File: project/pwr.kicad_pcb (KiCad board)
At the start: 2 copper layers, 75 x 80 mm, 113 parts, among them J101 IDC 2x8, J201 XT-IN, J202 METER, J203 XT-OUT, J301 XT-IN, J302 METER, J303 XT-OUT, J401 XT-IN, J402 METER, J403 XT-OUT, J501 XT-IN, J502 METER, J503 XT-OUT, J601 XT-IN, J602 METER, J603 XT-OUT, Q201 AON6144, Q301 AON6144, Q401 AON6144, Q501 AON6144, Q601 AON6144, U101 USBLC6-2SC6, U102 USBLC6-2SC6, U103 USBLC6-2SC6, U104 USBLC6-2SC6, U105 TMP102AIDRLR, U106 TMP102AIDRLR, U201 UCC27517DBVR, U301 UCC27517DBVR, U401 UCC27517DBVR, U501 UCC27517DBVR, U601 UCC27517DBVR

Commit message: finalizing design
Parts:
- removed kibuzzard-66D16323: G***, kibuzzard-66D16323
- added C108: 220u, Capacitor_SMD:CP_Elec_10x10.5, F.Cu at (121.0, 77.5)
- added D101: ALR, LED_SMD:LED_0805_2012Metric_Pad1.15x1.40mm_HandSolder, F.Cu at (129.5, 34.0)
- added D102: VCC, LED_SMD:LED_0805_2012Metric_Pad1.15x1.40mm_HandSolder, F.Cu at (115.5, 34.0)
- added R108: 100R, Resistor_SMD:R_0805_2012Metric_Pad1.20x1.40mm_HandSolder, F.Cu at (129.5, 36.0)
- added R109: 100R, Resistor_SMD:R_0805_2012Metric_Pad1.20x1.40mm_HandSolder, F.Cu at (115.5, 36.0)
- added TP101: TP_GND, TestPoint:TestPoint_Loop_D2.60mm_Drill1.6mm_Beaded, F.Cu at (124.0, 30.5)
- added TP201: TP_GND, TestPoint:TestPoint_Pad_D2.5mm, F.Cu at (151.0, 30.5)
- added TP301: TP_GND, TestPoint:TestPoint_Pad_D2.5mm, F.Cu at (151.0, 45.5)
- added TP401: TP_GND, TestPoint:TestPoint_Pad_D2.5mm, F.Cu at (151.0, 60.5)
- added TP501: TP_GND, TestPoint:TestPoint_Pad_D2.5mm, F.Cu at (151.0, 75.6)
- added TP601: TP_GND, TestPoint:TestPoint_Pad_D2.5mm, F.Cu at (151.0, 90.5)
- added kibuzzard-66D4F7A8: G***, kibuzzard-66D4F7A8, F.Cu at (174.2, 82.8)
- moved G102 21.0 mm to (109.0, 33.5)
- moved kibuzzard-66D08EDB 20.8 mm to (109.0, 87.5)
- moved G101 14.3 mm to (126.0, 87.5)
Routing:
- net 3V3: track 88.2 -> 123.4 mm, vias 10 -> 11
- net /ALERT_P: track 39.0 -> 54.5 mm, vias 3 -> 5
- net Net-(D102-Pad1): track 0.00 -> 2.01 mm
- net Net-(D101-Pad2): track 0.00 -> 2.01 mm
- net GND: vias 17 -> 24
- net /pwr_ch5/PGND: vias 7 -> 8
- net /pwr_ch4/PGND: vias 7 -> 8
- net /pwr_ch3/PGND: vias 7 -> 8
- net /pwr_ch2/PGND: vias 7 -> 8
- net /pwr_ch1/PGND: vias 7 -> 8
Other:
- board size 75 x 80 mm -> 75 x 77.5 mm
- board text added: "3V3"
- board text added: "JLCJLCJLCJL"
- board text added: "OTP"

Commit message: generating production files for power board
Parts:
- moved J101 28.0 mm to (121.5, 88.6)
- moved C101 28.0 mm to (134.2, 92.8)
- moved C102 28.0 mm to (132.2, 72.5)
- moved C103 28.0 mm to (132.2, 78.0)
- moved C104 28.0 mm to (132.2, 83.5)
- moved C105 28.0 mm to (132.2, 89.0)
- moved C106 28.0 mm to (140.5, 67.0)
- moved C107 28.0 mm to (140.5, 97.0)
- moved C108 28.0 mm to (126.0, 105.0)
- moved C201 28.0 mm to (144.5, 68.0)
- moved C202 28.0 mm to (140.5, 61.0)
- moved C203 28.0 mm to (148.5, 66.0)
- moved C204 28.0 mm to (148.5, 70.0)
- moved C301 28.0 mm to (144.5, 83.0)
- moved C302 28.0 mm to (140.5, 76.0)
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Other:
- board text added: "D = 3.2 mm"

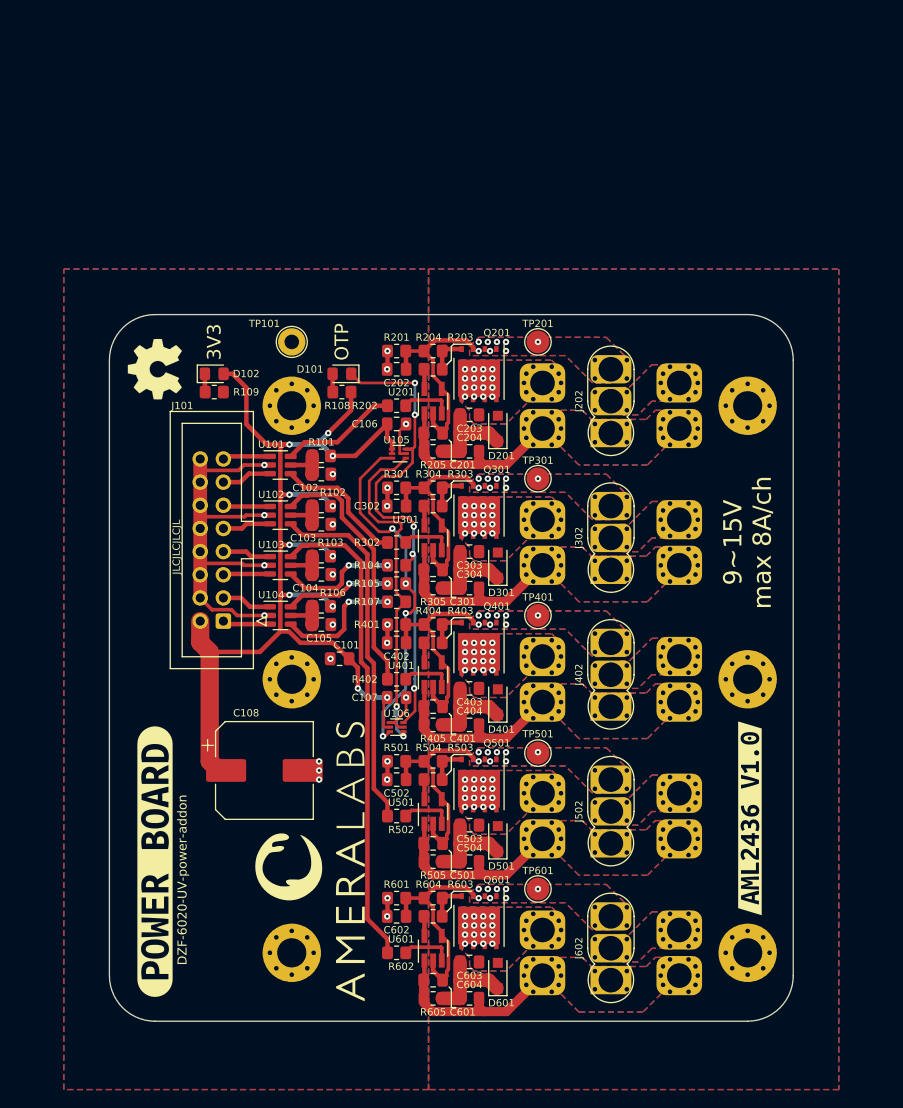
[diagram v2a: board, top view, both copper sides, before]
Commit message: adding user interface board
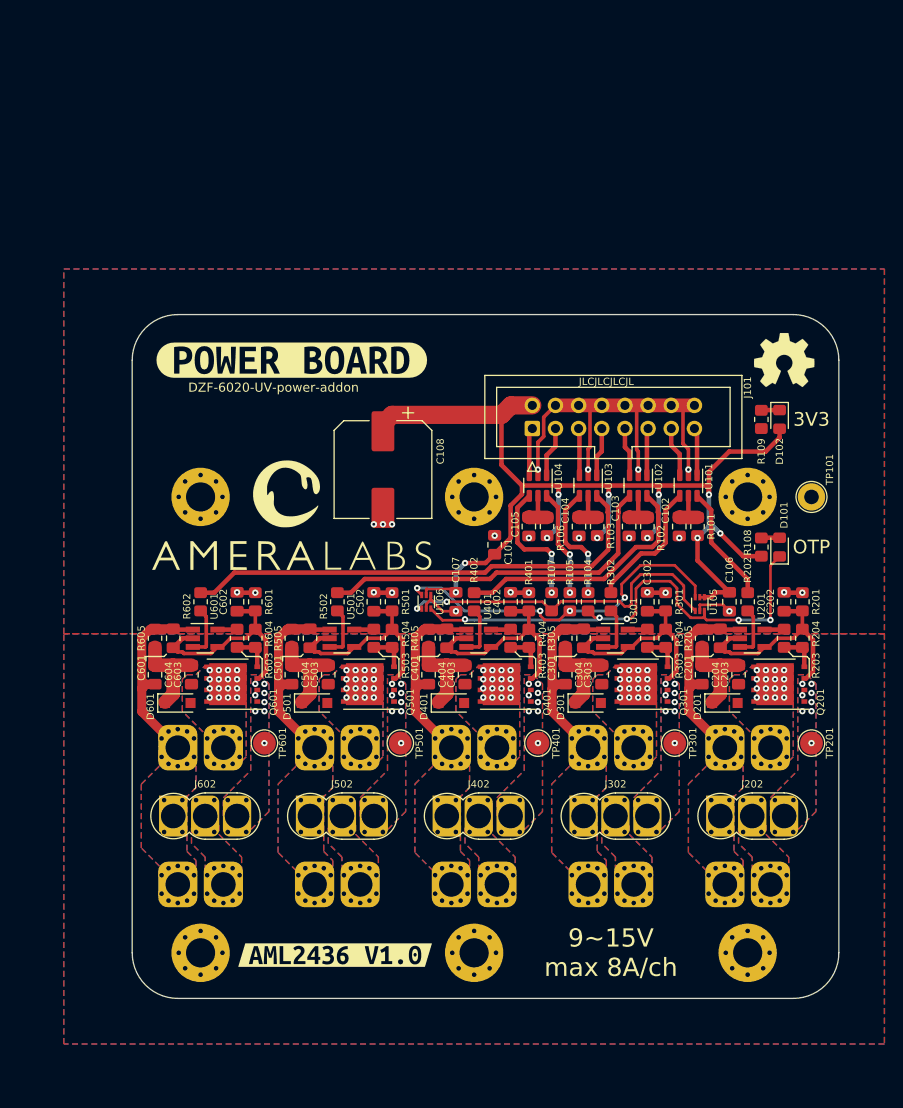
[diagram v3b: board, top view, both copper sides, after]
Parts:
- moved kibuzzard-66D17CEB 73.2 mm to (164.0, 125.0), turned to 180 degrees
- moved G102 69.0 mm to (183.0, 60.0), turned to 0 degrees
- moved kibuzzard-66D17D7D 63.6 mm to (176.0, 96.0), turned to 180 degrees
- moved D102 62.2 mm to (182.5, 66.5), turned to -90 degrees
- moved R109 60.1 mm to (180.5, 66.5), turned to 90 degrees
- moved H101 60.0 mm to (179.0, 125.0), turned to -90 degrees
- moved H104 60.0 mm to (119.0, 125.0), turned to -90 degrees
- moved TP101 59.5 mm to (186.0, 75.0), turned to -90 degrees
- moved kibuzzard-66D08EDB 57.0 mm to (129.0, 60.0), turned to 0 degrees
- moved J201 55.9 mm to (181.5, 117.5), turned to 180 degrees
- moved TP201 53.3 mm to (186.0, 102.0), turned to -90 degrees
- moved R201 52.3 mm to (185.0, 86.5), turned to -90 degrees
- moved D101 51.6 mm to (182.5, 80.5), turned to 90 degrees
- moved R204 51.3 mm to (185.0, 90.5), turned to 90 degrees
- moved J602 51.3 mm to (116.0, 110.0), turned to 180 degrees
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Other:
- board size 75 x 77.5 mm -> 77.5 x 75 mm

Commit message: fixing a lot of stuff in power board
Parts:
- removed the C204 at (174.0, 94.5)
- removed the C304 at (159.0, 94.5)
- removed the C404 at (144.0, 94.5)
- removed the C504 at (129.0, 94.5)
- removed the C604 at (114.0, 94.5)
- removed the H101 at (179.0, 125.0)
- removed the H103 at (149.0, 125.0)
- removed R205, R305, R405, R505, R605: 0, Resistor_SMD:R_0805_2012Metric_Pad1.20x1.40mm_HandSolder
- removed kibuzzard-66D17D7D: G***, kibuzzard-66D17D7D
- removed kibuzzard-66D17DB1: G***, kibuzzard-66D17DB1
- removed kibuzzard-66D17DB9: G***, kibuzzard-66D17DB9
- removed kibuzzard-66D17DC1: G***, kibuzzard-66D17DC1
- removed kibuzzard-66D17DC7: G***, kibuzzard-66D17DC7
- removed kibuzzard-66D4F7A8: G***, kibuzzard-66D4F7A8
- added C201: 10u/35v, Capacitor_SMD:C_1206_3216Metric_Pad1.33x1.80mm_HandSolder, F.Cu at (179.0, 120.0)
- added C203: 10u/35v, Capacitor_SMD:C_1206_3216Metric_Pad1.33x1.80mm_HandSolder, F.Cu at (184.5, 115.0)
- added C205: 10u/35v, Capacitor_SMD:C_1206_3216Metric_Pad1.33x1.80mm_HandSolder, F.Cu at (174.6, 93.0)
- added C301: 10u/35v, Capacitor_SMD:C_1206_3216Metric_Pad1.33x1.80mm_HandSolder, F.Cu at (164.0, 120.0)
- added C303: 10u/35v, Capacitor_SMD:C_1206_3216Metric_Pad1.33x1.80mm_HandSolder, F.Cu at (169.5, 115.0)
- added C305: 10u/35v, Capacitor_SMD:C_1206_3216Metric_Pad1.33x1.80mm_HandSolder, F.Cu at (159.6, 93.0)
- added C401: 10u/35v, Capacitor_SMD:C_1206_3216Metric_Pad1.33x1.80mm_HandSolder, F.Cu at (149.0, 120.0)
- added C403: 10u/35v, Capacitor_SMD:C_1206_3216Metric_Pad1.33x1.80mm_HandSolder, F.Cu at (154.5, 115.0)
- added C405: 10u/35v, Capacitor_SMD:C_1206_3216Metric_Pad1.33x1.80mm_HandSolder, F.Cu at (144.6, 93.0)
- added C501: 10u/35v, Capacitor_SMD:C_1206_3216Metric_Pad1.33x1.80mm_HandSolder, F.Cu at (134.0, 120.0)
- added C503: 10u/35v, Capacitor_SMD:C_1206_3216Metric_Pad1.33x1.80mm_HandSolder, F.Cu at (139.5, 115.0)
- added C505: 10u/35v, Capacitor_SMD:C_1206_3216Metric_Pad1.33x1.80mm_HandSolder, F.Cu at (129.6, 93.0)
- added C601: 10u/35v, Capacitor_SMD:C_1206_3216Metric_Pad1.33x1.80mm_HandSolder, F.Cu at (119.0, 120.0)
- added C603: 10u/35v, Capacitor_SMD:C_1206_3216Metric_Pad1.33x1.80mm_HandSolder, F.Cu at (124.5, 115.0)
- added C605: 10u/35v, Capacitor_SMD:C_1206_3216Metric_Pad1.33x1.80mm_HandSolder, F.Cu at (114.6, 93.0)
- added H105: MountingHole_Pad, MountingHole:MountingHole_3.2mm_M3_Pad_Via, F.Cu at (119.0, 125.0)
- added H106: MountingHole_Pad, MountingHole:MountingHole_3.2mm_M3_Pad_Via, F.Cu at (149.0, 125.0)
- added kibuzzard-6705D8EF: G***, kibuzzard-6705D8EF, F.Cu at (133.8, 125.2)
- added kibuzzard-6705D925: G***, kibuzzard-6705D925, B.Cu at (119.5, 94.0)
- added kibuzzard-6705D93C: G***, kibuzzard-6705D93C, B.Cu at (134.5, 94.0)
- added kibuzzard-6705D966: G***, kibuzzard-6705D966, B.Cu at (149.5, 94.0)
- added kibuzzard-6705D971: G***, kibuzzard-6705D971, B.Cu at (164.5, 94.0)
- added kibuzzard-6705D97C: G***, kibuzzard-6705D97C, B.Cu at (179.5, 94.0)
- C202, C302, C402, C502, C602: value 100n -> 10u/35v; footprint Capacitor_SMD:C_0805_2012Metric_Pad1.18x1.45mm_HandSolder -> Capacitor_SMD:C_1206_3216Metric_Pad1.33x1.80mm_HandSolder
- D201, D301, D401, D501, D601: value DS14W -> SS34A; footprint Diode_SMD:D_SOD-123F -> Diode_SMD:D_SMA
- R109: value 100R -> 1K
- R201, R301, R401, R501, R601: value 10K -> 10R
- R203, R303, R403, R503, R603: value 43R -> 33R
- moved H104 60.0 mm to (179.0, 125.0), turned to 0 degrees
- moved C202 28.8 mm to (179.0, 115.0), turned to 0 degrees
- moved C302 28.8 mm to (164.0, 115.0), turned to 0 degrees
- moved C402 28.8 mm to (149.0, 115.0), turned to 0 degrees
- moved C502 28.8 mm to (134.0, 115.0), turned to 0 degrees
- moved C602 28.8 mm to (119.0, 115.0), turned to 0 degrees
- moved kibuzzard-66D17D14 28.8 mm to (177.5, 87.0)
- moved C206 4.06 mm to (174.0, 95.2), turned to 0 degrees
- moved C306 4.06 mm to (159.0, 95.2), turned to 0 degrees
- moved C406 4.06 mm to (144.0, 95.2), turned to 0 degrees
- moved C506 4.06 mm to (129.0, 95.2), turned to 0 degrees
- moved C606 4.06 mm to (114.0, 95.2), turned to 0 degrees
- moved D201 1.08 mm to (175.5, 98.0)
- moved D301 1.08 mm to (160.5, 98.0)
- moved D401 1.08 mm to (145.5, 98.0)
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- renumbered C201 to C204, C203 to C206, C301 to C304, C303 to C306, C401 to C404, C403 to C406, C501 to C504, C503 to C506, C601 to C604, C603 to C606, H106 to H101, H105 to H103
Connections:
- C202 pad 1: /pwr_ch1/PGND -> /pwr_ch1/Vcc
- C202 pad 2: GND -> /pwr_ch1/IN-
- C206 pad 1: /pwr_ch1/snub -> /pwr_ch1/Vcc
- C302 pad 1: /pwr_ch2/PGND -> /pwr_ch2/Vcc
- C302 pad 2: GND -> /pwr_ch2/IN-
- C306 pad 1: /pwr_ch2/snub -> /pwr_ch2/Vcc
- C402 pad 1: /pwr_ch3/PGND -> /pwr_ch3/Vcc
- C402 pad 2: GND -> /pwr_ch3/IN-
- C406 pad 1: /pwr_ch3/snub -> /pwr_ch3/Vcc
- C502 pad 1: /pwr_ch4/PGND -> /pwr_ch4/Vcc
- C502 pad 2: GND -> /pwr_ch4/IN-
- C506 pad 1: /pwr_ch4/snub -> /pwr_ch4/Vcc
- C602 pad 1: /pwr_ch5/PGND -> /pwr_ch5/Vcc
- C602 pad 2: GND -> /pwr_ch5/IN-
- C606 pad 1: /pwr_ch5/snub -> /pwr_ch5/Vcc
- D201 pad 1: /pwr_ch1/snub -> /pwr_ch1/Vcc
- D301 pad 1: /pwr_ch2/snub -> /pwr_ch2/Vcc
- D401 pad 1: /pwr_ch3/snub -> /pwr_ch3/Vcc
- D501 pad 1: /pwr_ch4/snub -> /pwr_ch4/Vcc
- D601 pad 1: /pwr_ch5/snub -> /pwr_ch5/Vcc
- H104 pad 1: GND -> unconnected-(H104-Pad1)
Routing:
- net /pwr_ch1/Vcc: track 21.4 -> 4.36 mm, vias 0 -> 18
- net /pwr_ch5/Vcc: track 21.4 -> 4.40 mm, vias 0 -> 28
- net /pwr_ch4/Vcc: track 21.4 -> 4.40 mm, vias 0 -> 28
- net /pwr_ch3/Vcc: track 21.4 -> 4.40 mm, vias 0 -> 28
- net /pwr_ch2/Vcc: track 21.4 -> 4.40 mm, vias 0 -> 28
- net /pwr_ch5/snub: track 10.4 -> 0.00 mm
- net /pwr_ch4/snub: track 10.4 -> 0.00 mm
- net /pwr_ch3/snub: track 10.4 -> 0.00 mm
- net /pwr_ch2/snub: track 10.4 -> 0.00 mm
- net /pwr_ch1/snub: track 10.4 -> 0.00 mm
- net GND: track 69.4 -> 59.7 mm, vias 24 -> 23
- net /SDA_P: track 39.2 -> 37.2 mm, vias 4 -> 2
- net /ALERT_P: track 54.5 -> 53.0 mm, vias 5 -> 3
- net Net-(R107-Pad1): track 14.2 -> 13.1 mm
- net Net-(R104-Pad1): track 13.0 -> 12.0 mm
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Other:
- board text added: "10~14V max 8A/ch"
- board text removed: "9~15V max 8A/ch"
- board text removed: "JLCJLCJLCJL"

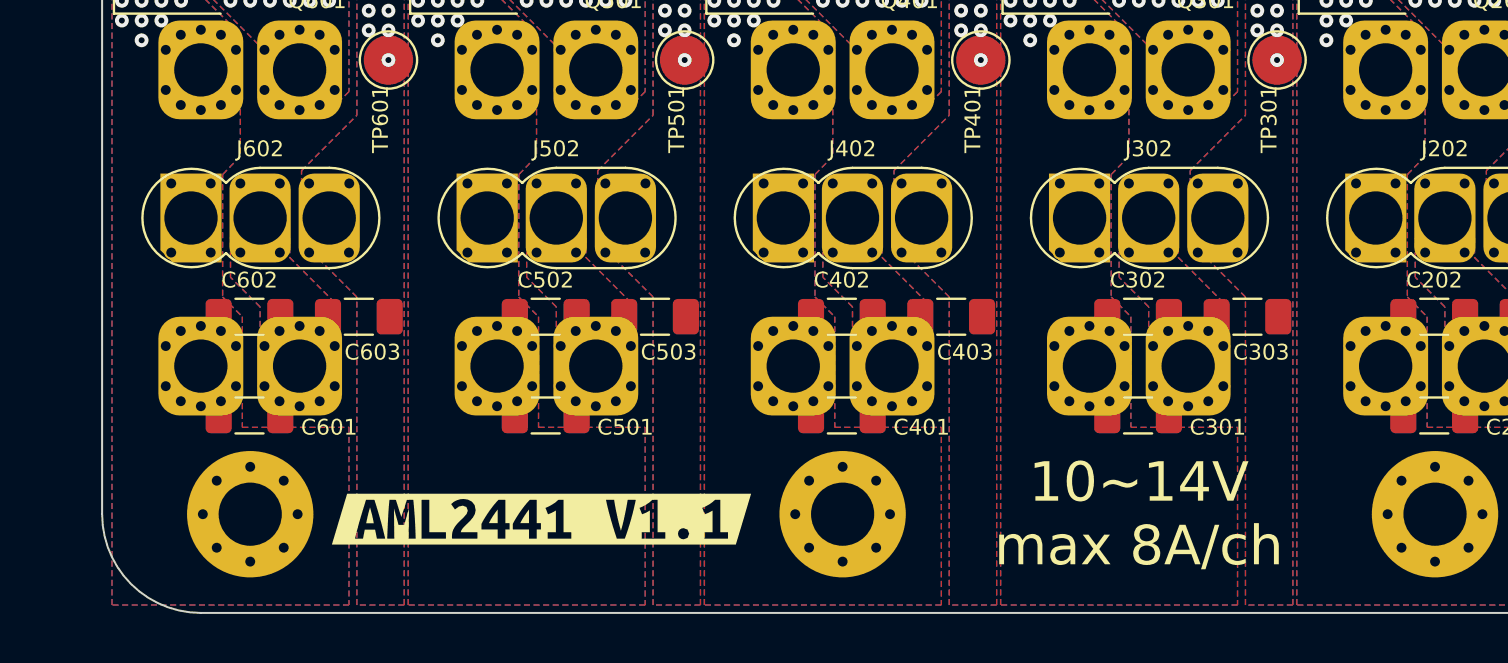
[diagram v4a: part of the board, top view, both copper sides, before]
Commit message: rs485 connector and minor silkscreen and led values fixes
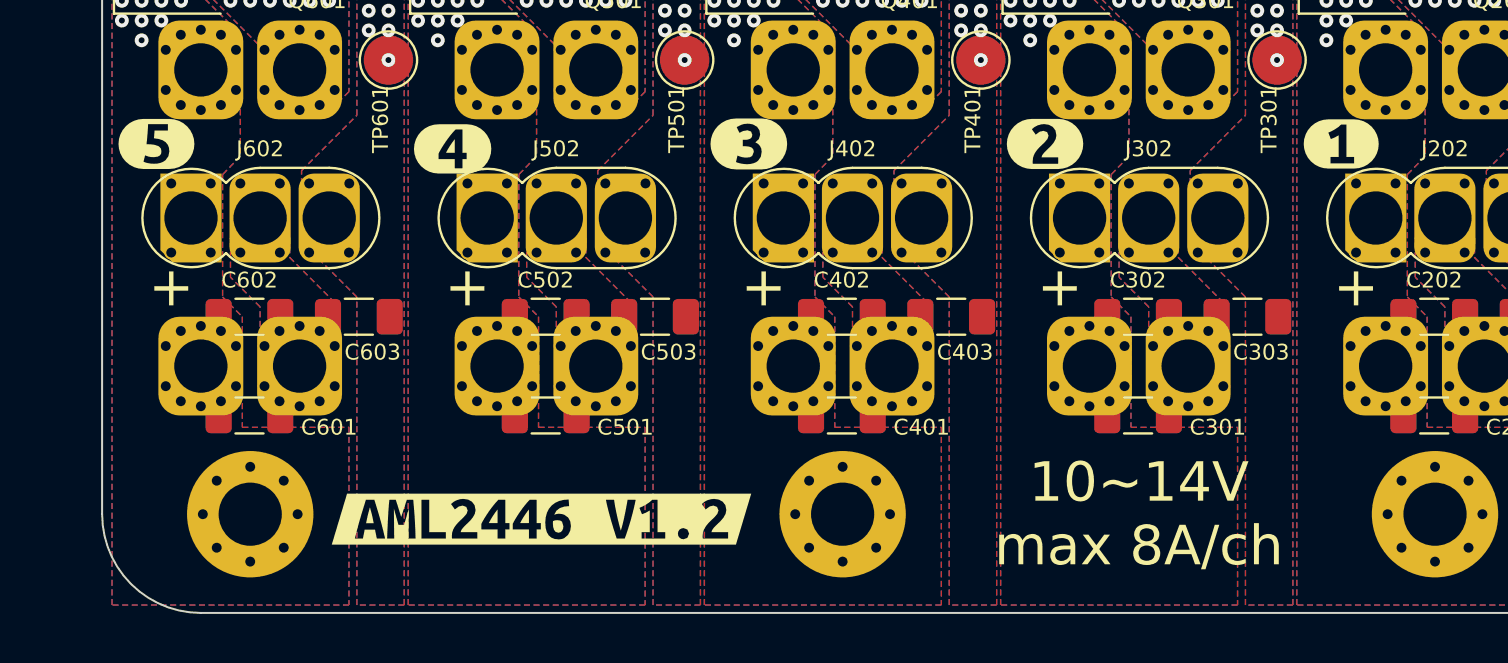
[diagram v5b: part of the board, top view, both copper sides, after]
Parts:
- removed kibuzzard-6705D8EF: G***, kibuzzard-6705D8EF
- added kibuzzard-6736C30A: G***, kibuzzard-6736C30A, F.Cu at (133.8, 125.2)
- added kibuzzard-6736C676: G***, kibuzzard-6736C676, F.Cu at (174.2, 106.2)
- added kibuzzard-6736C6C3: G***, kibuzzard-6736C6C3, F.Cu at (159.2, 106.2)
- added kibuzzard-6736C6D1: G***, kibuzzard-6736C6D1, F.Cu at (144.2, 106.2)
- added kibuzzard-6736C6DD: G***, kibuzzard-6736C6DD, F.Cu at (129.2, 106.5)
- added kibuzzard-6736C6EF: G***, kibuzzard-6736C6EF, F.Cu at (114.2, 106.2)
- D101: value ALR -> OTP
- R109: value 1K -> 4k7
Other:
- board text added: "+"
